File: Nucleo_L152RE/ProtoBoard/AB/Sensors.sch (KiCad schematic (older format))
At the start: 59 parts, among them P12 USART2, P13 SWD Header, P14 RGB1, P15 USART1, P16 MS1, P17 MS3, P18 MS2, P19 MS4, P20 WS1, P21 OW1_A, P22 I2C1_A, P23 I2C2_A, P24 WS2, P25 I2C1_B, P26 I2C2_B, P27 SW_1_6, P28 WS3, P29 OW2_A, P30 OW3_A, SW1 MomentarySwitch, SW2 MomentarySwitch

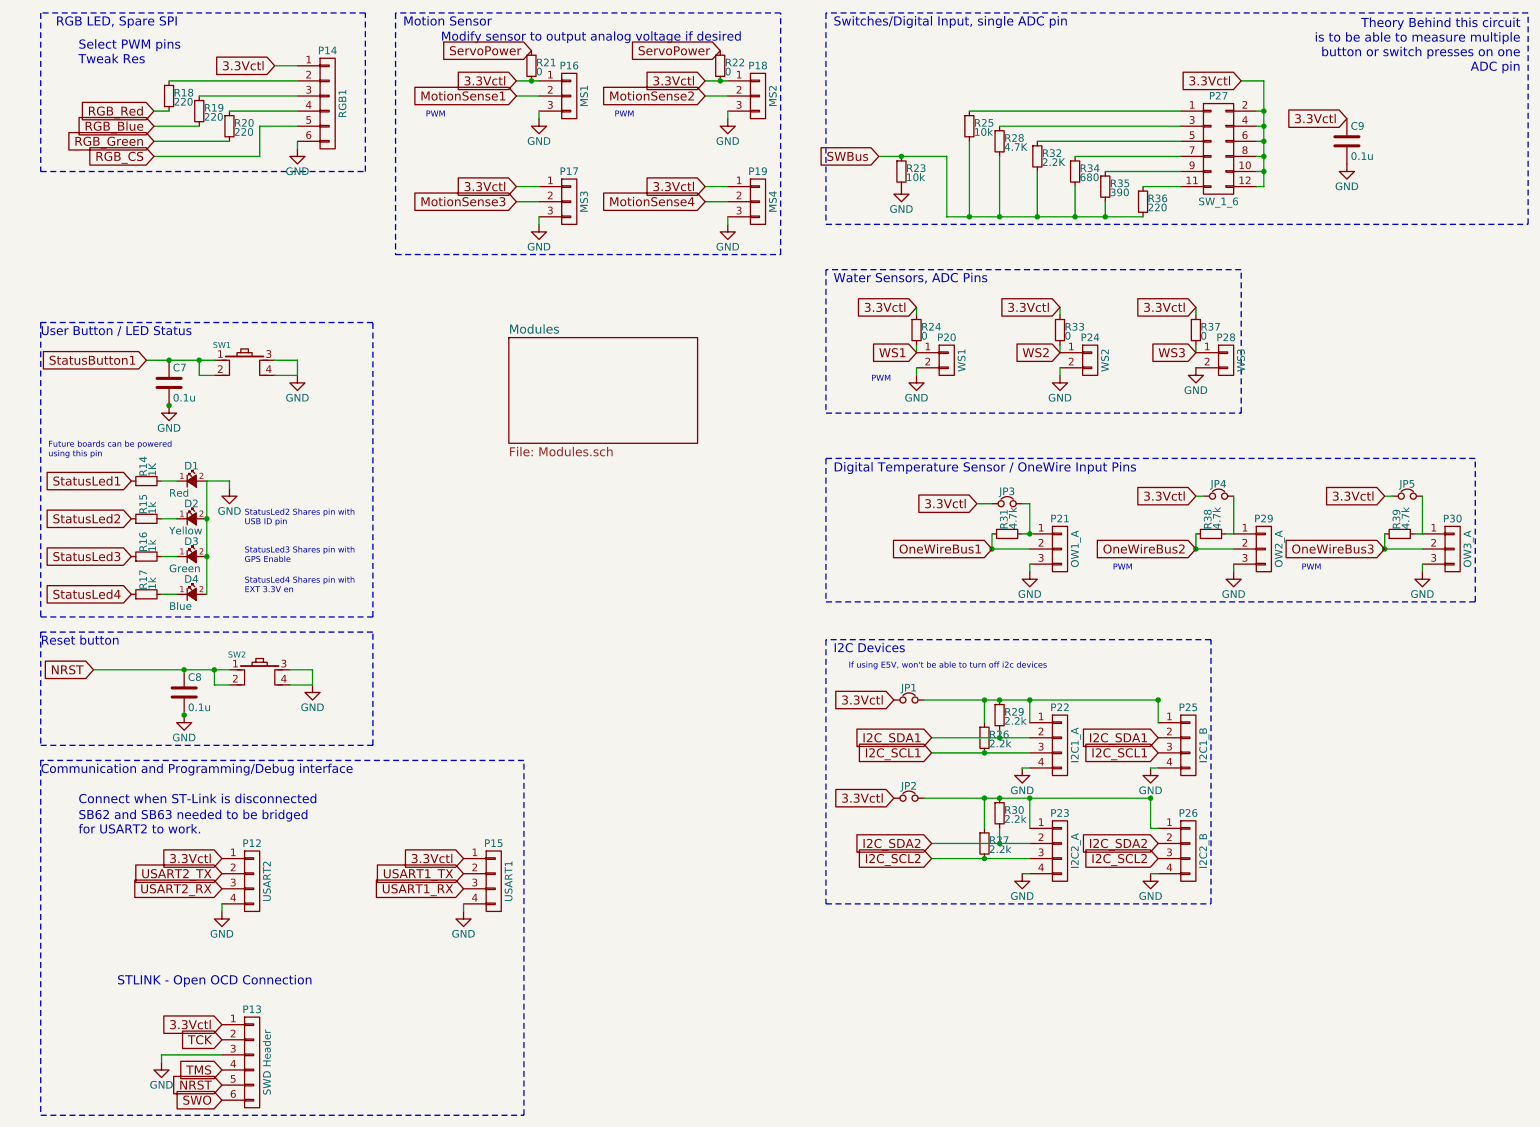
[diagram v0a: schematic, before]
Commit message: Components mostly laid out into final resting positions with exception of plethora of single pin connections for easily connecting to GND, 3.3V, 5V, 3.3Vctl.
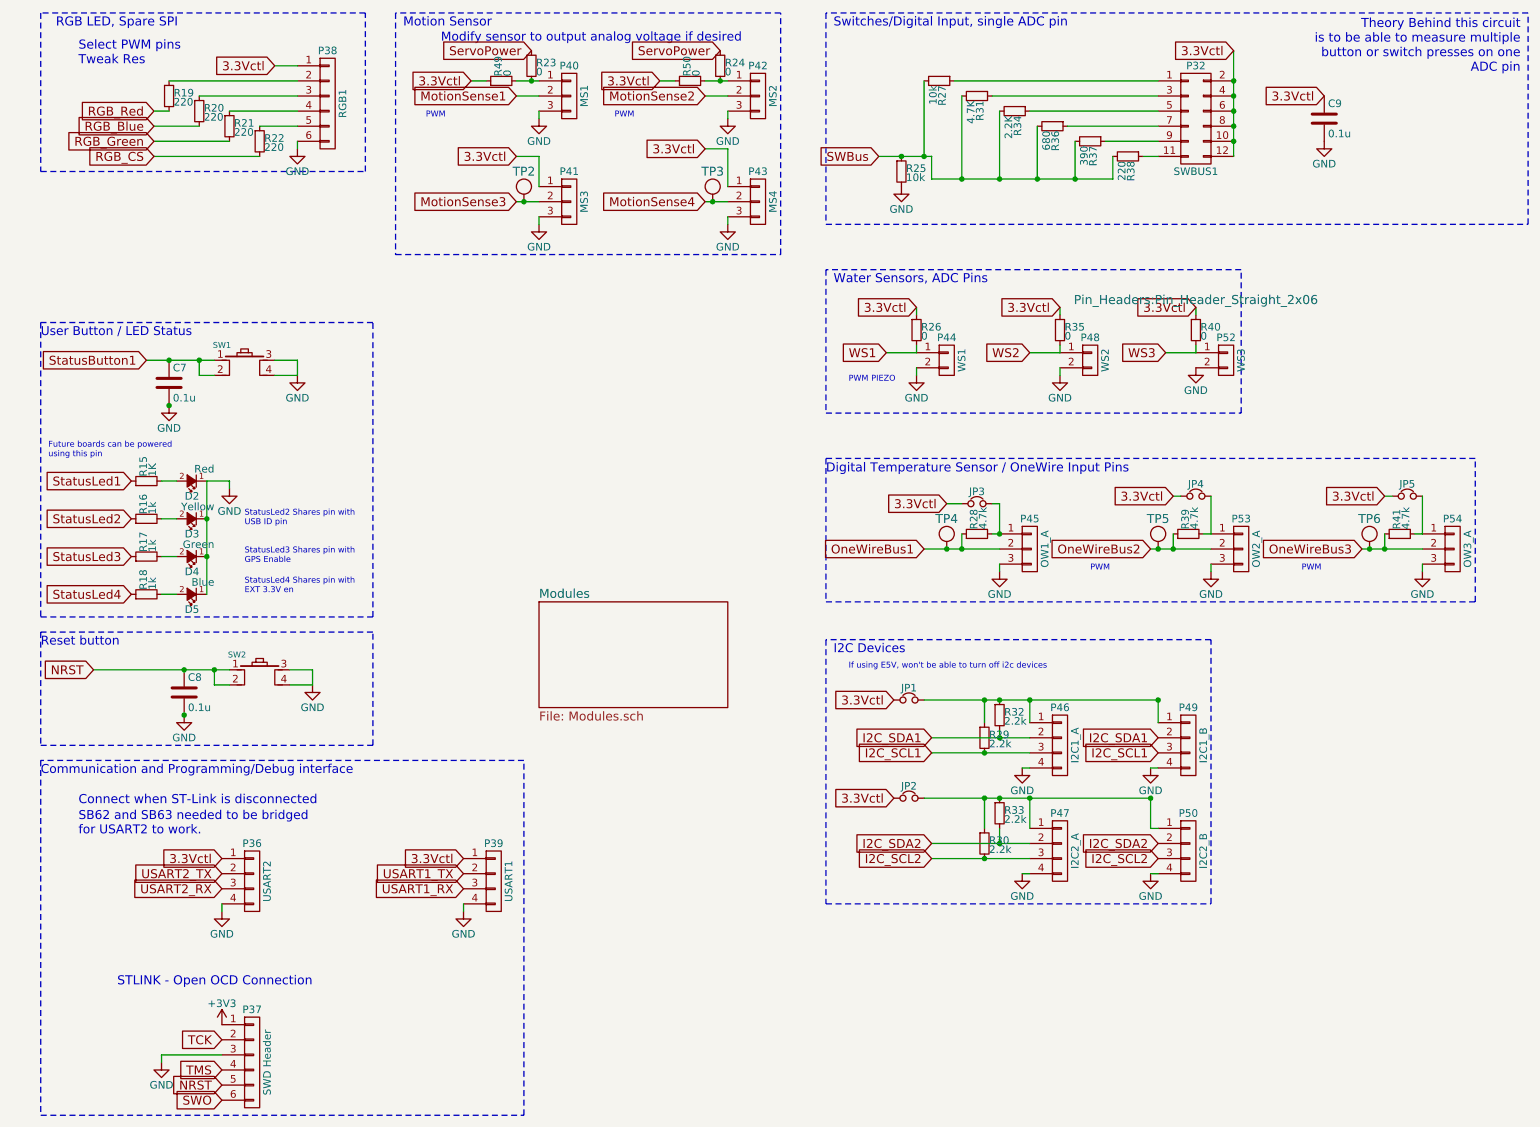
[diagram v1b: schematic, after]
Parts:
- removed P27: SW_1_6, Pin_Headers:Pin_Header_Straight_2x06, symbol CONN_02X06
- added P32: SWBUS1, Pin_Headers:Pin_Header_Straight_2x06, symbol CONN_02X06
- added R22: 220, Resistors_SMD:R_0603_HandSoldering, symbol R_Small
- added R49, R50: 0, Resistors_SMD:R_0603_HandSoldering, symbol R_Small
- added TP2, TP3, TP4, TP5, TP6: tp, nucleo:TestPoint_1mm, symbol tp
- D2: renamed from D1; footprint nucleo:LED_0603 -> nucleo:LED_0603_Standard
- D3: renamed from D2; footprint nucleo:LED_0603 -> nucleo:LED_0603_Standard
- D4: renamed from D3; footprint nucleo:LED_0603 -> nucleo:LED_0603_Standard
- D5: renamed from D4; footprint nucleo:LED_0603 -> nucleo:LED_0603_Standard
- JP1, JP2, JP3, JP4, JP5: footprint nucleo:SB_NC -> nucleo:SB_NC_Smaller
- P38: renamed from P14; footprint (none) -> Pin_Headers:Pin_Header_Straight_1x06
- SW2: value MomentarySwitch -> ResetSwitch
- renumbered P12 to P36, P13 to P37, P15 to P39, P16 to P40, P17 to P41, P18 to P42, P19 to P43, P20 to P44, P21 to P45, P22 to P46, P23 to P47, P24 to P48, P25 to P49, P26 to P50, P28 to P52, P29 to P53, P30 to P54, R14 to R15, R15 to R16, R16 to R17, R17 to R18, R18 to R19, R19 to R20, R20 to R21, R21 to R23, R22 to R24, R23 to R25, R24 to R26, R25 to R27, R31 to R28, R26 to R29, R27 to R30, R28 to R31, R29 to R32, R30 to R33, R32 to R34, R33 to R35, R34 to R36, R35 to R37, R36 to R38, R38 to R39, R37 to R40, R39 to R41
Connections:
- net 3.3Vctl: now also P32.10 (P10), P32.12 (P12), P32.2 (P2), P32.4 (P4), P32.6 (P6), P32.8 (P8), R49.1, R50.1; no longer P37.1 (P1), P40.1 (P1), P42.1 (P1), R23.2, R24.2
- net GND: now also D2.1 (K), D3.1 (K), D4.1 (K), D5.1 (K); no longer D2.2 (A), D3.2 (A), D4.2 (A), D5.2 (A)
- net MotionSense3: now also TP2.1
- net MotionSense4: now also TP3.1
- net OneWireBus1: now also TP4.1
- net OneWireBus2: now also TP5.1
- net OneWireBus3: now also TP6.1
- net RGB_CS: now also R22.2; no longer P38.5 (P5)
- net at R27.1: now also P32.1 (P1)
- net at R38.1: now also P32.11 (P11)
- net at R31.1: now also P32.3 (P3)
- net at R34.1: now also P32.5 (P5)
- net at R36.1: now also P32.7 (P7)
- net at R37.1: now also P32.9 (P9)
- net at R15.2: now also D2.2 (A); no longer D2.1 (K)
- net at R16.2: now also D3.2 (A); no longer D3.1 (K)
- net at R17.2: now also D4.2 (A); no longer D4.1 (K)
- net at R18.2: now also D5.2 (A); no longer D5.1 (K)
- new net: P40.1 (P1), R23.2, R49.2
- new net: P42.1 (P1), R24.2, R50.2
- new net: P38.5 (P5), R22.1
- new net +3V3: P37.1 (P1)
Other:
- note added: "PIEZO"
- moved on the sheet: C9, JP3, JP4, P45, P53, R27, R28, R31, R34, R36, R37, R38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

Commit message: Added many traces which will have to be removed since I put via's on pads :/
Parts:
- JP1, JP2, JP3, JP4, JP5: footprint nucleo:SB_NC_Smaller -> nucleo:SB_NO_Smaller; symbol Jumper_NC_Small -> Jumper_Small
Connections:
- net 3.3Vctl: now also JP1.2, JP2.2, JP3.2, JP4.2, JP5.2, P45.1 (P1), P46.1 (P1), P47.1 (P1), P49.1 (P1), P50.1 (P1), P53.1 (P1), P54.1 (P1), R28.2, R29.1, R30.1, R32.1, R33.1, R39.2, R41.2
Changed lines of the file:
@@
 $EndComp
 $Comp
-L Jumper_NC_Small JP2
+L Jumper_Small JP2
 U 1 1 555AC273
 P 6350 5750
 F 0 "JP2" H 6350 5830 50  0000 C CNN
 F 1 "Jumper_NC_Small" H 6360 5690 50  0001 C CNN
-F 2 "nucleo:SB_NC_Smaller" H 6350 5750 60  0001 C CNN
+F 2 "nucleo:SB_NO_Smaller" H 6350 5750 60  0001 C CNN
 F 3 "" H 6350 5750 60  0000 C CNN
 	1    6350 5750
@@
 $EndComp
 $Comp
-L Jumper_NC_Small JP1
+L Jumper_Small JP1
 U 1 1 555AC27A
 P 6350 5100
 F 0 "JP1" H 6350 5180 50  0000 C CNN
 F 1 "Jumper_NC_Small" H 6360 5040 50  0001 C CNN
-F 2 "nucleo:SB_NC_Smaller" H 6350 5100 60  0001 C CNN
+F 2 "nucleo:SB_NO_Smaller" H 6350 5100 60  0001 C CNN
 F 3 "" H 6350 5100 60  0000 C CNN
 	1    6350 5100
@@
 $EndComp
 $Comp
-L Jumper_NC_Small JP3
+L Jumper_Small JP3
 U 1 1 555AC2C9
 P 6800 3800
 F 0 "JP3" H 6800 3880 50  0000 C CNN
 F 1 "Jumper_NC_Small" H 6810 3740 50  0001 C CNN
-F 2 "nucleo:SB_NC_Smaller" H 6800 3800 60  0001 C CNN
+F 2 "nucleo:SB_NO_Smaller" H 6800 3800 60  0001 C CNN
 F 3 "" H 6800 3800 60  0000 C CNN
 	1    6800 3800
@@
 $EndComp
 $Comp
-L Jumper_NC_Small JP5
+L Jumper_Small JP5
 U 1 1 555AC2D6
 P 9650 3750
 F 0 "JP5" H 9650 3830 50  0000 C CNN
 F 1 "Jumper_NC_Small" H 9660 3690 50  0001 C CNN
-F 2 "nucleo:SB_NC_Smaller" H 9650 3750 60  0001 C CNN
+F 2 "nucleo:SB_NO_Smaller" H 9650 3750 60  0001 C CNN
 F 3 "" H 9650 3750 60  0000 C CNN
 	1    9650 3750
@@
 $EndComp
 $Comp
-L Jumper_NC_Small JP4
+L Jumper_Small JP4
 U 1 1 555AC2E3
 P 8250 3750
 F 0 "JP4" H 8250 3830 50  0000 C CNN
 F 1 "Jumper_NC_Small" H 8260 3690 50  0001 C CNN
-F 2 "nucleo:SB_NC_Smaller" H 8250 3750 60  0001 C CNN
+F 2 "nucleo:SB_NO_Smaller" H 8250 3750 60  0001 C CNN
 F 3 "" H 8250 3750 60  0000 C CNN
 	1    8250 3750
@@
 Connection ~ 6950 5100
 Wire Wire Line
-	6450 5750 7950 5750
-Wire Wire Line
-	6450 5100 8000 5100
+	6250 5750 7950 5750
+Wire Wire Line
+	6250 5100 8000 5100
 Wire Wire Line
 	8250 2750 8250 2800
@@
 3.3Vctl
 Wire Wire Line
-	6950 4000 6950 3800
-Wire Wire Line
-	6950 3800 6900 3800
-Wire Wire Line
-	6600 3800 6700 3800
+	6950 3800 6950 4000
+Wire Wire Line
+	6600 3800 6950 3800
 Text GLabel 9500 3750 0    59   Input ~ 0
 3.3Vctl
 Wire Wire Line
-	9550 3750 9500 3750
+	9500 3750 9750 3750
 Text GLabel 8100 3750 0    59   Input ~ 0
 3.3Vctl
 Wire Wire Line
-	8150 3750 8100 3750
+	8100 3750 8350 3750
 Text GLabel 2150 900  0    59   Input ~ 0
 3.3Vctl
@@
 Connection ~ 8500 1100
 Connection ~ 8500 1000
+Connection ~ 9550 3750
+Connection ~ 8150 3750
+Connection ~ 6900 3800
+Connection ~ 6700 3800
+Connection ~ 6450 5100
+Connection ~ 6450 5750
 $EndSCHEMATC

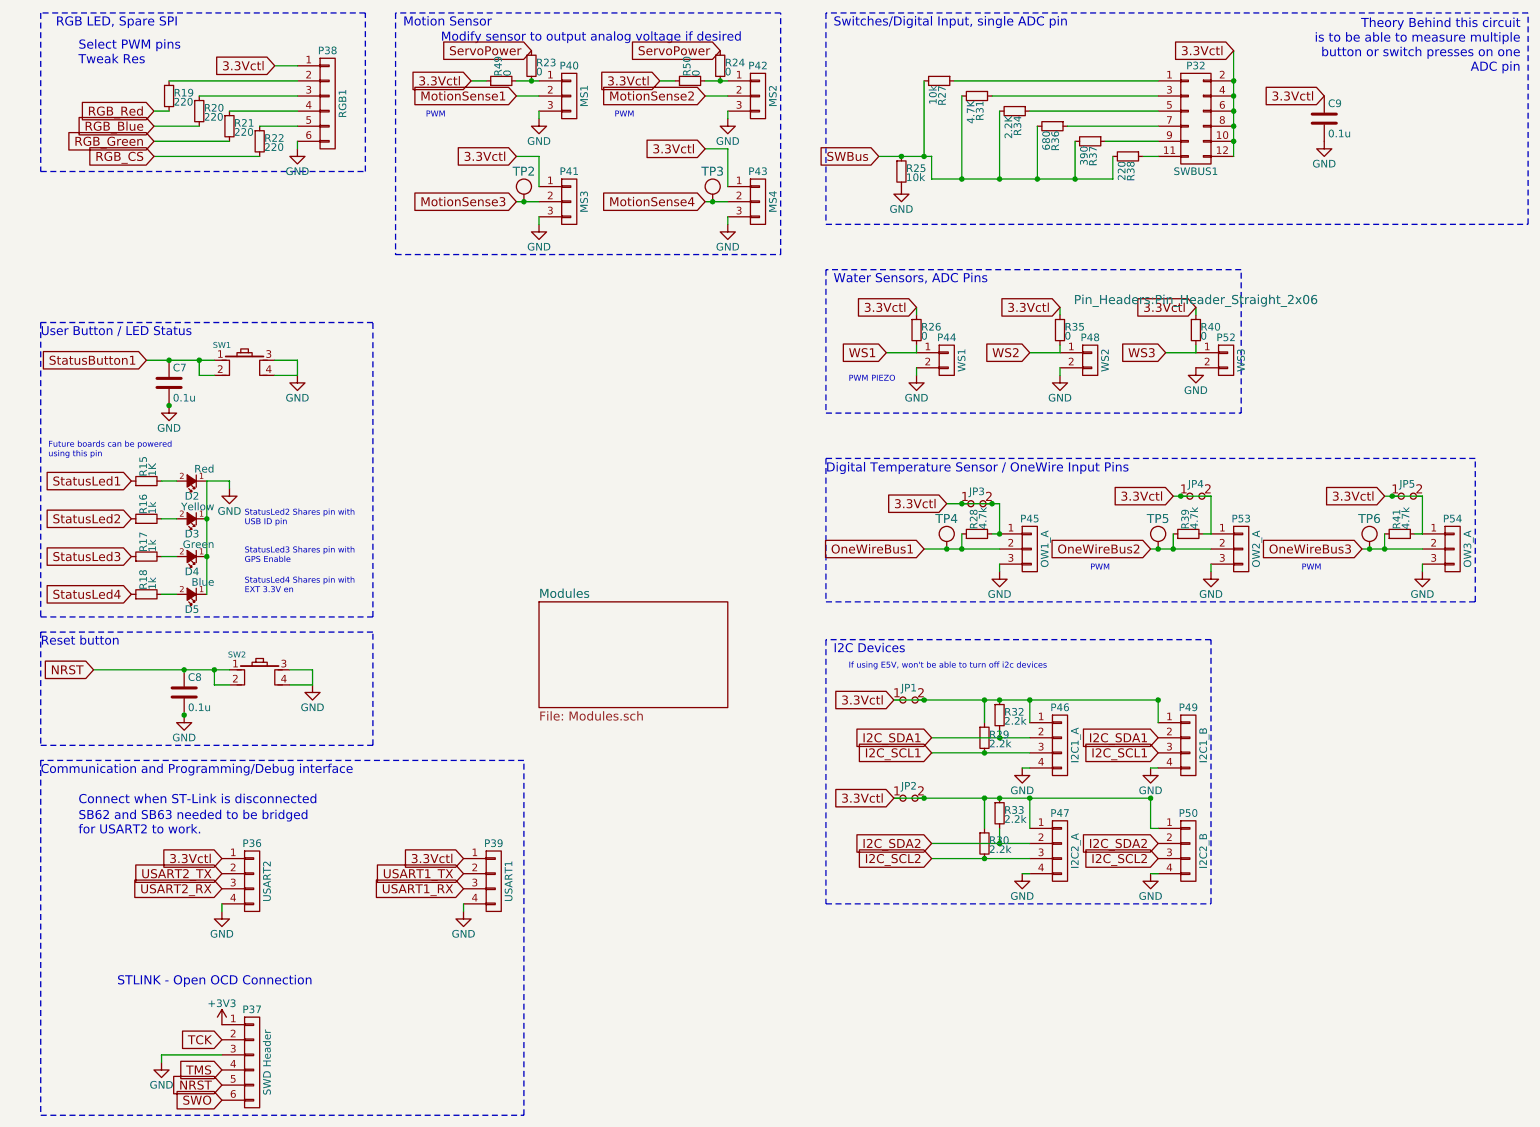
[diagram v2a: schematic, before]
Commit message: Final draft with all traces and artwork in place.
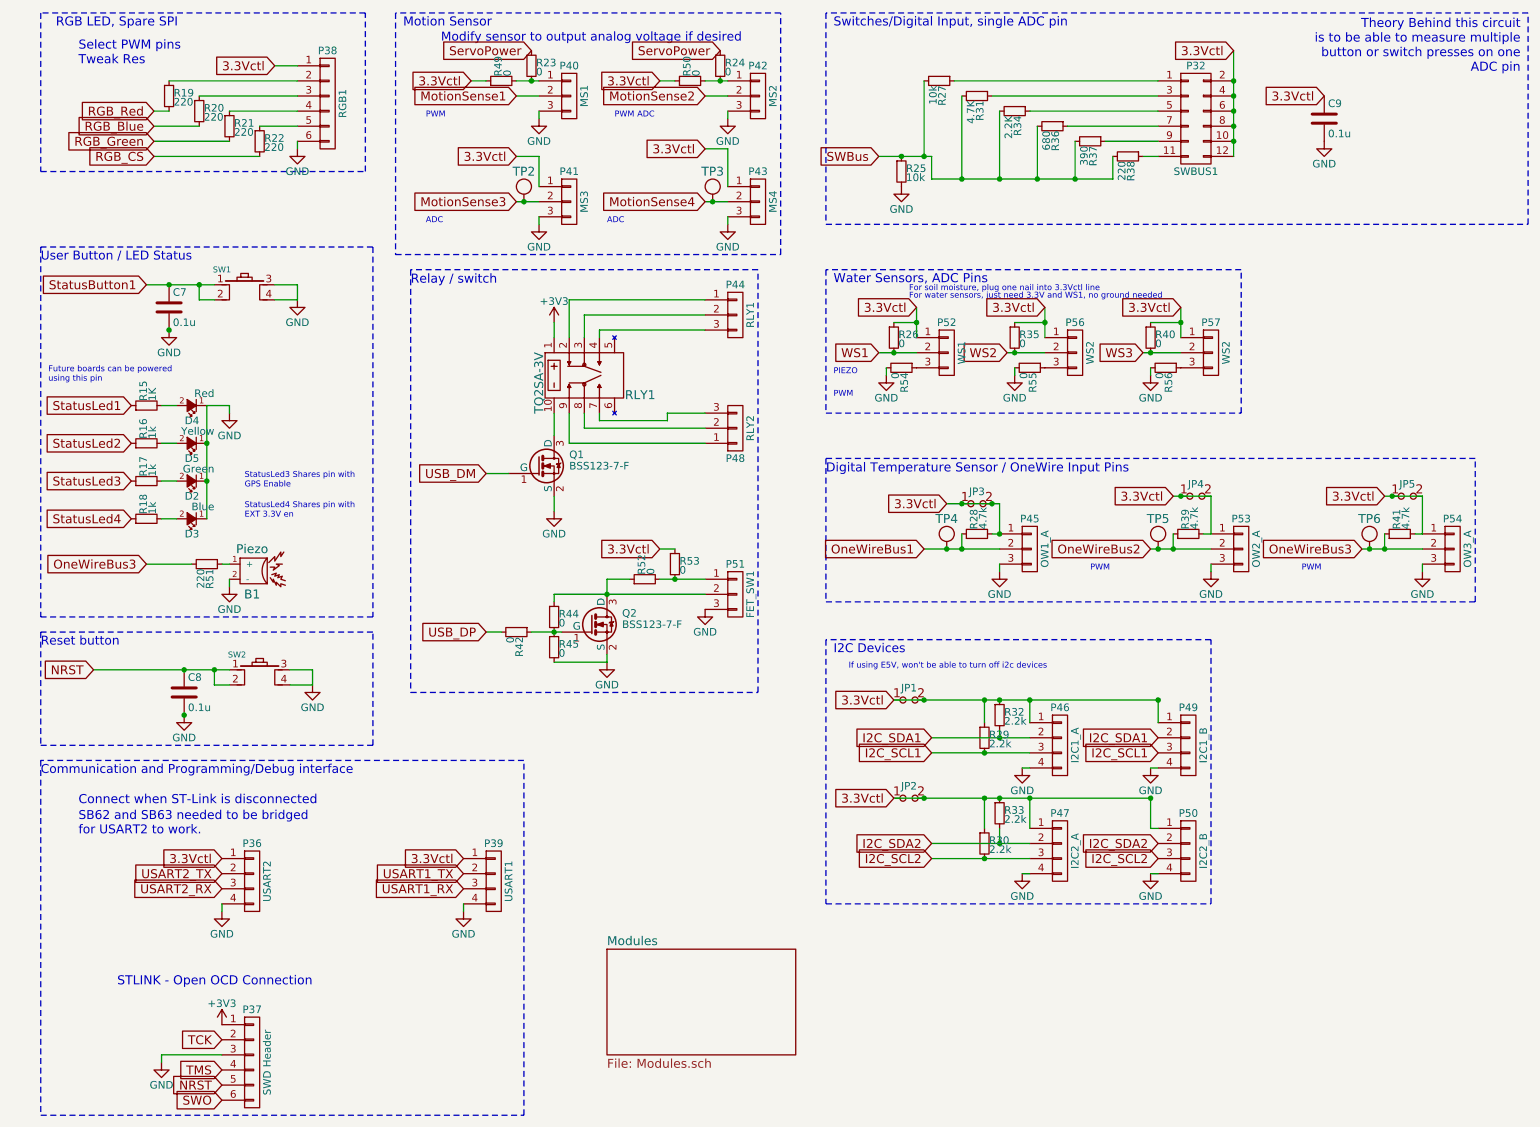
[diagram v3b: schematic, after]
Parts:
- removed P44: WS1, Pin_Headers:Pin_Header_Straight_1x02, symbol CONN_01X02
- removed P48: WS2, Pin_Headers:Pin_Header_Straight_1x02, symbol CONN_01X02
- removed P52: WS3, Pin_Headers:Pin_Header_Straight_1x02, symbol CONN_01X02
- added B1: Piezo, nucleo:Piezo_12mm, symbol Piezo
- added P44: RLY1, Pin_Headers:Pin_Header_Straight_1x03, symbol CONN_01X03
- added P48: RLY2, Pin_Headers:Pin_Header_Straight_1x03, symbol CONN_01X03
- added P51: FET_SW1, Pin_Headers:Pin_Header_Straight_1x03, symbol CONN_01X03
- added P52: WS1, Pin_Headers:Pin_Header_Straight_1x03, symbol CONN_01X03
- added P56, P57: WS2, Pin_Headers:Pin_Header_Straight_1x03, symbol CONN_01X03
- added Q1, Q2: BSS123-7-F, nucleo:SOT23-3, symbol BSS123
- added R42, R44, R45, R52, R53, R54, R55, R56: 0, Resistors_SMD:R_0603_HandSoldering, symbol R_Small
- added R51: 220, Resistors_SMD:R_0603_HandSoldering, symbol R_Small
- added RLY1: TQ2SA-3V, nucleo:Relay_SMD, symbol Relay
- renumbered D4 to D2, D5 to D3, D2 to D4, D3 to D5
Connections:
- net +3V3: now also RLY1.1
- net 3.3Vctl: now also P52.1 (P1), P56.1 (P1), P57.1 (P1), R53.1
- net GND: now also B1.2 (-), P51.3 (P3), Q1.2 (S), Q2.2 (S), R45.2, R54.2, R55.2, R56.2
- net OneWireBus3: now also R51.2
- net WS1: now also P52.2 (P2)
- net WS2: now also P56.2 (P2)
- net WS3: now also P57.2 (P2)
- new net: B1.1 (+), R51.1
- new net: Q1.3 (D), RLY1.10
- new net: P44.1 (P1), RLY1.2
- new net: P44.2 (P2), RLY1.3
- new net: P44.3 (P3), RLY1.4
- new net: P48.3 (P3), RLY1.7
- new net: P48.2 (P2), RLY1.8
- new net: P48.1 (P1), RLY1.9
- new net: Q2.1 (G), R42.1, R44.2, R45.1
- new net: P51.2 (P2), Q2.3 (D), R44.1, R52.1
- new net: P51.1 (P1), R52.2, R53.2
- new net: P52.3 (P3), R54.1
- new net: P56.3 (P3), R55.1
- new net: P57.3 (P3), R56.1
- new net USB_DM: Q1.1 (G)
- new net USB_DP: R42.2
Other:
- note added: "ADC"
- note added: "For soil moisture, plug one nail into 3.3Vctl line"
- note added: "For water sensors, just need 3.3V and WS1, no ground needed"
- note added: "Relay / switch\n\n"
- note removed: "StatusLed2 Shares pin with \nUSB ID pin"
- moved on the sheet: C7, D2, D3, D4, D5, R15, R16, R17, R18, R26, R35, R40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
